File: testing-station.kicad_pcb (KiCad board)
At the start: 2 copper layers, 212.7 x 113.3 mm, 80 parts, among them IC1 BME680, IC2 DS3231, IC3 74HC4050D, J1 pyranometer, J13 microSD, J2 anemometer, J3 AM2315C, J4 FPC connector, J5 Pt100, J7 Pt100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

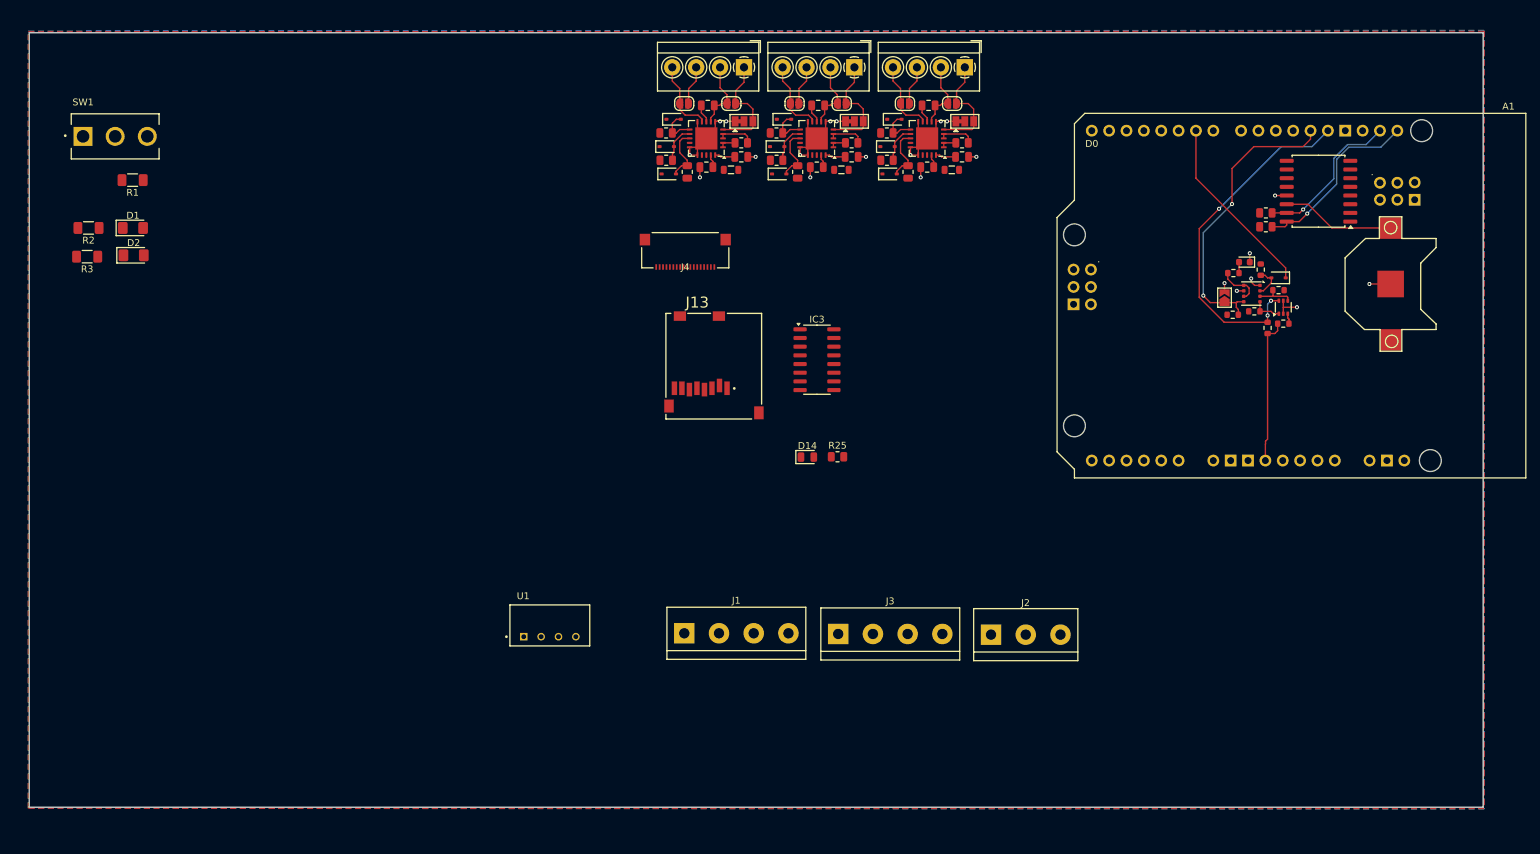
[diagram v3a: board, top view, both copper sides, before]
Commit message: changed Arduino symbol to connectors only
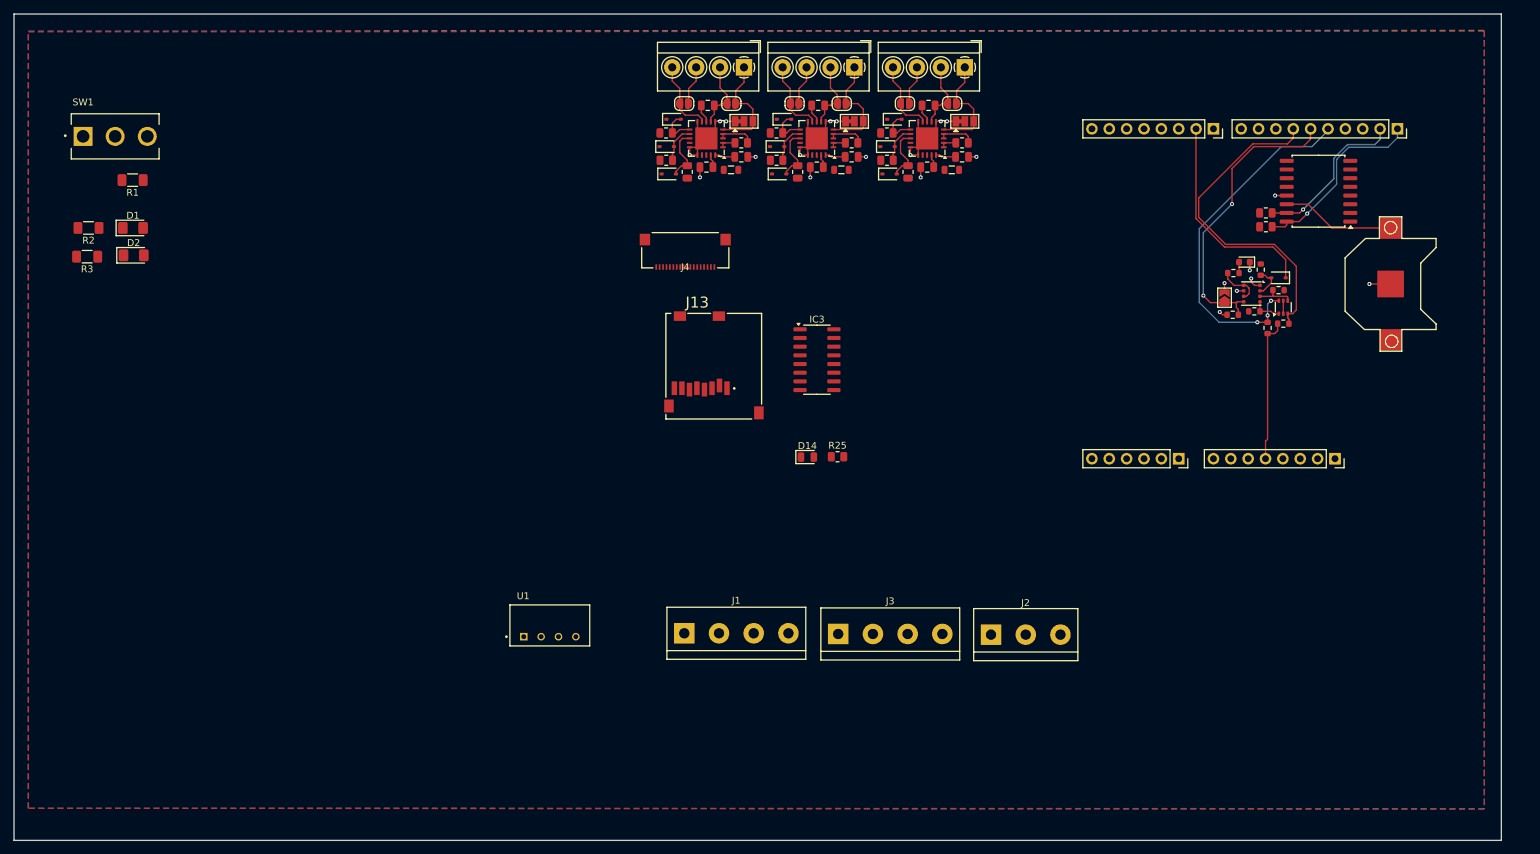
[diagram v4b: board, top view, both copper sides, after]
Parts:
- removed A1: Arduino_Uno_R4_WiFi_Shield, PCM_arduino-library:Arduino_Uno_R4_WiFi_Shield
- added J10: Conn_01x06_Socket, Connector_PinSocket_2.54mm:PinSocket_1x06_P2.54mm_Vertical, F.Cu at (209.8, 83.9)
- added J11: Conn_01x08_Socket, Connector_PinSocket_2.54mm:PinSocket_1x08_P2.54mm_Vertical, F.Cu at (232.7, 83.9)
- added J6: Conn_01x10_Socket, Connector_PinSocket_2.54mm:PinSocket_1x10_P2.54mm_Vertical, F.Cu at (241.8, 35.6)
- added J8: Conn_01x08_Socket, Connector_PinSocket_2.54mm:PinSocket_1x08_P2.54mm_Vertical, F.Cu at (214.9, 35.6)
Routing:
- net /MOSI: track 1.52 -> 48.3 mm
- net /D6: track 27.0 -> 31.1 mm
- net /SCA: track 22.5 -> 23.6 mm
- net /SCL: track 26.6 -> 27.5 mm
- net +3.3V: track 15.9 -> 15.1 mm
- net /MISO: track 44.0 -> 43.2 mm
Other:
- board size 212.7 x 113.3 mm -> 217.6 x 120.9 mm

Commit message: finished routing
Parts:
- J1, J3: footprint TerminalBlock:TerminalBlock_bornier-4_P5.08mm -> TerminalBlock_4Ucon:TerminalBlock_4Ucon_1x04_P3.50mm_Horizontal
- J2: footprint TerminalBlock:TerminalBlock_bornier-3_P5.08mm -> TerminalBlock_4Ucon:TerminalBlock_4Ucon_1x03_P3.50mm_Horizontal
- moved SW1 124.4 mm to (174.9, 67.0)
- moved R1 124.2 mm to (177.6, 71.9)
- moved R3 123.8 mm to (173.7, 61.8)
- moved R2 123.7 mm to (173.7, 59.2)
- moved D1 122.5 mm to (179.0, 59.2)
- moved D2 122.3 mm to (179.0, 61.8)
- moved JP3 85.2 mm to (217.4, 61.3), turned to -90 degrees
- moved D3 83.3 mm to (215.2, 59.8), turned to -90 degrees
- moved C3 83.0 mm to (217.2, 64.8), turned to 90 degrees
- moved JP2 81.6 mm to (217.4, 68.2), turned to -90 degrees
- moved R6 81.5 mm to (213.2, 58.7), turned to 90 degrees
- moved U1 80.1 mm to (188.7, 71.1)
- moved D4 79.0 mm to (211.2, 58.8), turned to -90 degrees
- moved JP1 77.3 mm to (214.8, 70.1), turned to -90 degrees
- moved U2 76.8 mm to (212.3, 64.5), turned to 90 degrees
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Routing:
- net +5V: track 21.1 -> 142.7 mm, vias 0 -> 3
- net /MISO: track 43.2 -> 144.5 mm, vias 2 -> 7
- net +9V: track 0.00 -> 100.2 mm
- net /A5: track 0.00 -> 92.4 mm
- net /SCL: track 27.5 -> 119.7 mm, vias 1 -> 3
- net /D9: track 0.00 -> 82.1 mm, vias 0 -> 2
- net /SCK: track 51.3 -> 127.6 mm, vias 3 -> 8
- net /D4: track 0.00 -> 69.8 mm, vias 0 -> 4
- net /MOSI: track 48.3 -> 115.7 mm, vias 0 -> 9
- net /D8: track 0.00 -> 59.5 mm, vias 0 -> 5
- net Net-(J5-Pin_4): track 10.9 -> 62.5 mm, vias 0 -> 3
- net Net-(J5-Pin_2): track 10.0 -> 59.2 mm
- net /D2: track 0.00 -> 48.7 mm, vias 0 -> 3
- net /microSD/3Y: track 0.00 -> 48.6 mm, vias 0 -> 2
- net /microSD/2Y: track 0.00 -> 48.1 mm, vias 0 -> 2
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- added copper zone on In2.Cu, net +3.3V
- added copper zone on In1.Cu, net GND
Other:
- board size 217.6 x 120.9 mm -> 108.5 x 54.1 mm
- copper layers 2 -> 4

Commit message: autorouting
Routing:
- net +9V: track 100.2 -> 56.8 mm
- net GND: track 94.2 -> 52.4 mm, vias 34 -> 16
- net /A5: track 92.4 -> 68.1 mm
- net /SCL: track 119.7 -> 142.6 mm, vias 3 -> 1
- net Net-(J5-Pin_4): track 62.5 -> 40.3 mm
- net /D9: track 82.1 -> 66.1 mm
- net /D4: track 69.8 -> 55.1 mm, vias 4 -> 1
- net +3.3V: track 29.9 -> 44.5 mm, vias 18 -> 28
- net /A2: track 31.2 -> 17.4 mm, vias 5 -> 1
- net /A1: track 39.5 -> 26.9 mm, vias 8 -> 1
- net /D2: track 48.7 -> 38.0 mm, vias 3 -> 1
- net /MISO: track 144.5 -> 153.1 mm, vias 7 -> 5
- net Net-(J5-Pin_2): track 59.2 -> 50.6 mm, vias 0 -> 3
- net /D6: track 36.8 -> 29.9 mm
- net Net-(J5-Pin_1): track 60.2 -> 53.5 mm, vias 2 -> 3
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- added copper zone on F.Cu, net GND
- removed copper zone on F.Cu, net +3.3V
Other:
- board size 108.5 x 54.1 mm -> 95 x 53.9 mm

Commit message: more compact format
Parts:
- moved J4 67.3 mm to (155.1, 108.5)
- moved J1 66.0 mm to (144.7, 106.8)
- moved J9 65.6 mm to (145.8, 83.9)
- moved J7 65.6 mm to (129.7, 83.9)
- moved J2 65.0 mm to (122.8, 124.0)
- moved J5 65.0 mm to (135.2, 124.0)
- moved IC2 64.0 mm to (190.6, 88.0)
- moved J10 64.0 mm to (163.3, 127.9)
- moved J6 64.0 mm to (195.3, 79.6)
- moved B1 64.0 mm to (195.2, 104.7)
- moved J11 64.0 mm to (186.1, 127.9)
- moved J8 64.0 mm to (168.3, 79.6)
- moved R23 64.0 mm to (182.9, 93.2)
- moved R24 64.0 mm to (182.9, 91.1)
- moved C2 61.8 mm to (165.2, 112.6)
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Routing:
- net /A5: track 68.1 -> 23.6 mm
- net /MISO: track 153.1 -> 119.2 mm, vias 5 -> 3
- net Net-(J9-Pin_1): track 23.6 -> 55.7 mm
- net /SCL: track 142.6 -> 111.4 mm
- net Net-(J9-Pin_4): track 32.6 -> 60.7 mm, vias 0 -> 1
- net +9V: track 56.8 -> 83.8 mm, vias 0 -> 1
- net /SCK: track 128.5 -> 102.9 mm, vias 2 -> 5
- net /D8: track 57.3 -> 32.1 mm, vias 1 -> 2
- net +5V: track 140.4 -> 116.6 mm, vias 3 -> 1
- net /microSD/3Y: track 51.1 -> 71.1 mm
- net /MOSI: track 117.9 -> 98.5 mm, vias 4 -> 1
- net /D2: track 38.0 -> 18.7 mm
- net /A2: track 17.4 -> 32.6 mm
- net Net-(D14-K): track 15.5 -> 2.73 mm
- net /D4: track 55.1 -> 67.6 mm
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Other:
- board size 95 x 53.9 mm -> 82.3 x 53.9 mm
- board text added: "fffff"
